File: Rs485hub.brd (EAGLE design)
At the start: 100 x 100 mm, 97 parts, among them IC1 SN75176PA, IC2 74AC00N, IC3 SN75176PA, IC4 74AC00N, IC5 SN75176PA, IC6 74AC00N, IC7 SN75176PA, IC8 74AC00N

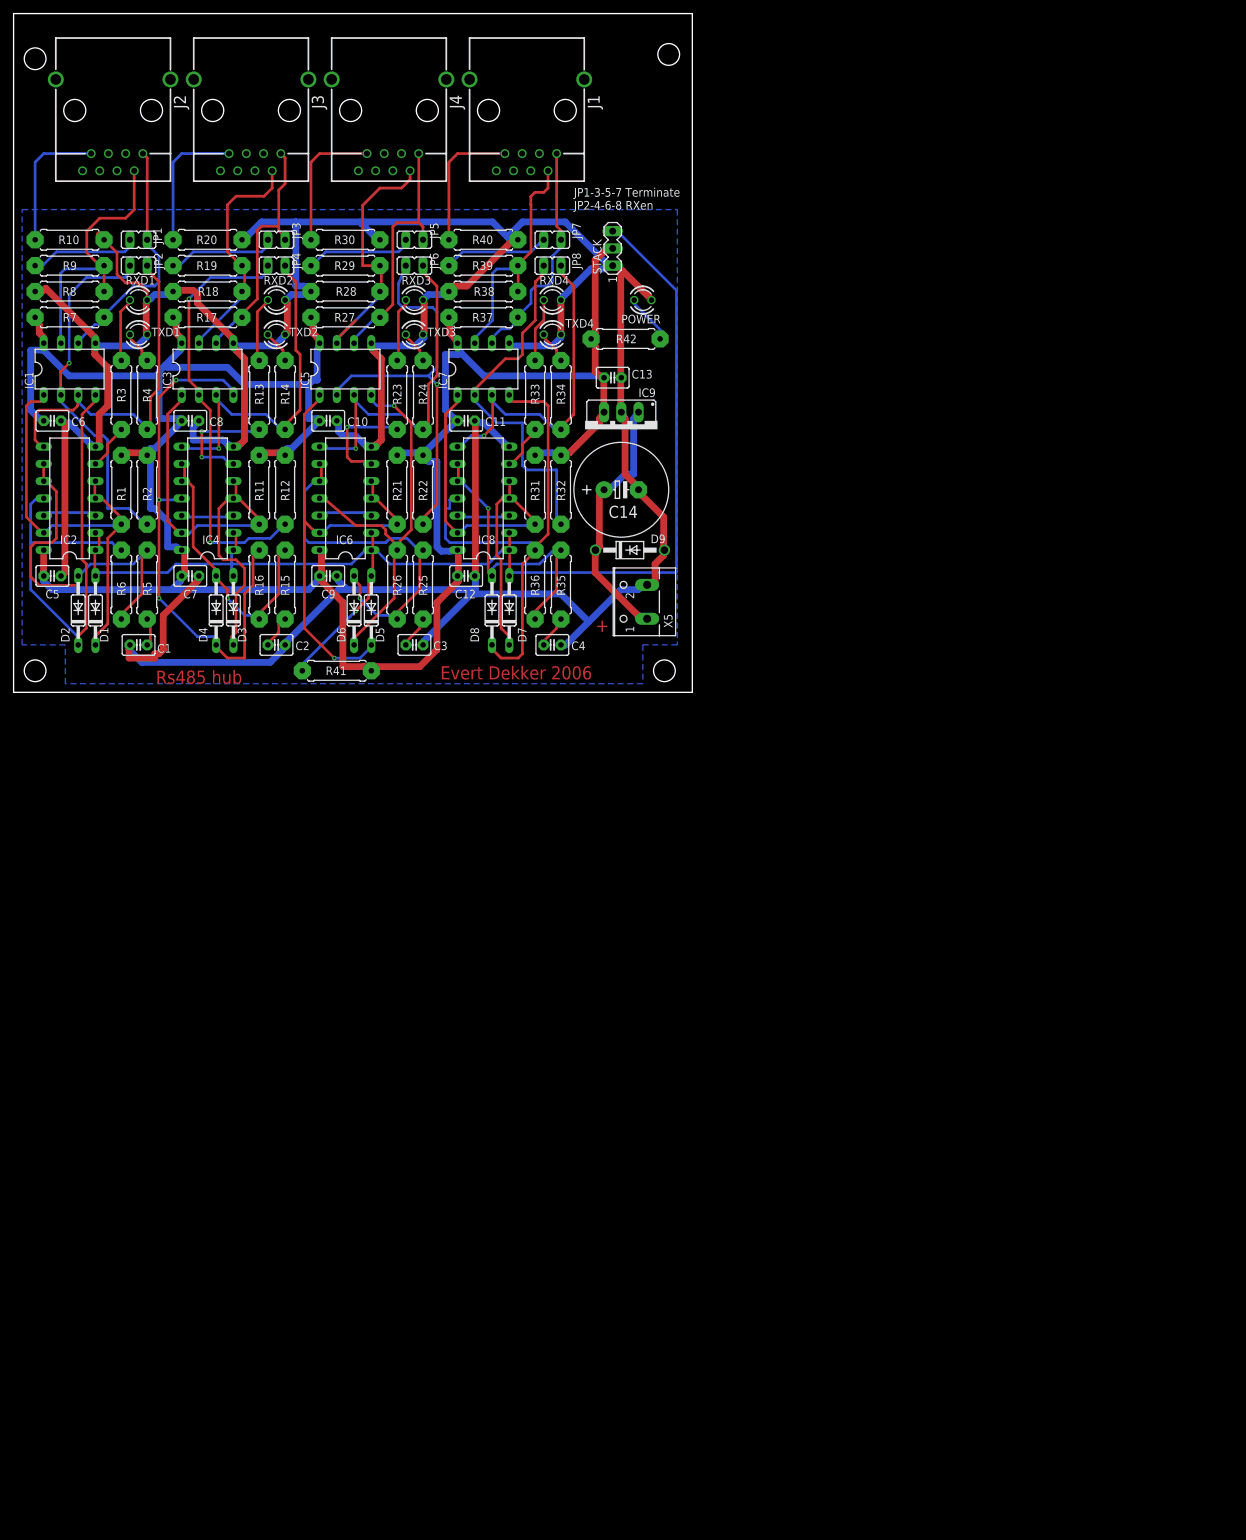
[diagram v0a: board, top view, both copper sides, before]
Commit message: Further mods for the 19" rack at RaumZeitLabor, still needs routing
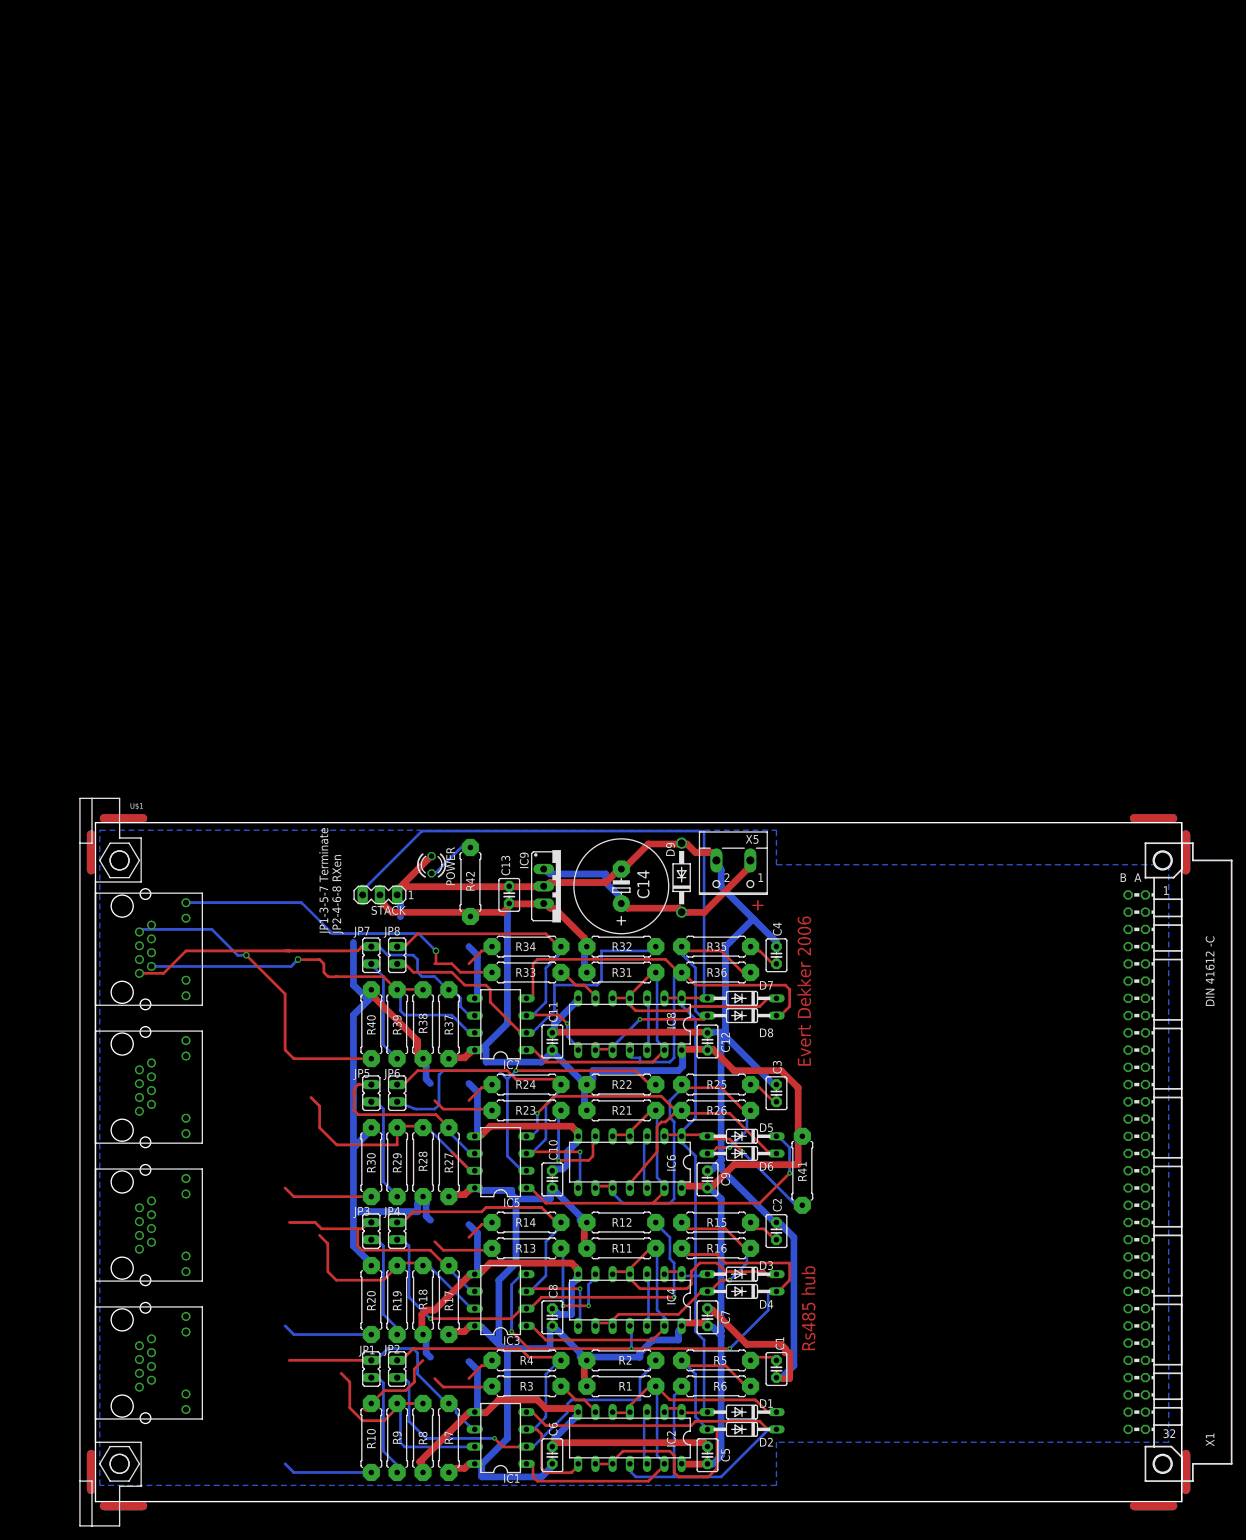
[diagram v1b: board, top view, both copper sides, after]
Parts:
- removed J1, J2, J3, J4: (no value), con-amp:557786-1
- removed RXD1, RXD2, RXD3, RXD4: Grn rxd, led:LED3MM
- removed TXD1, TXD2, TXD3, TXD4: red txd, led:LED3MM
- added U$1: (no value), 19inch:EK-FP
- added U$2, U$3, U$4, U$5: RJHS508, RJHS:P-RJHS-538X
- added X1: MAB64, con-vg:MAB64
- moved R10 182.0 mm to (52.7, -109.9), turned to 90 degrees
- moved R9 179.3 mm to (56.5, -109.9), turned to 90 degrees
- moved R8 176.8 mm to (60.3, -109.9), turned to 270 degrees
- moved R7 174.3 mm to (64.1, -109.9), turned to 90 degrees
- moved JP1 169.9 mm to (52.7, -99.7), turned to 180 degrees
- moved IC1 169.8 mm to (71.8, -109.9), turned to 90 degrees
- moved C6 169.3 mm to (79.4, -112.4), turned to 90 degrees
- moved JP2 167.0 mm to (56.5, -99.7), turned to 180 degrees
- moved C5 161.5 mm to (102.2, -112.4), turned to 90 degrees
- moved IC2 161.2 mm to (90.8, -109.9), turned to 180 degrees
- moved R20 158.1 mm to (52.7, -89.5), turned to 90 degrees
- moved R3 157.8 mm to (75.6, -102.2), turned to 0 degrees
- moved D2 155.3 mm to (107.3, -108.6), turned to 180 degrees
- moved R19 154.9 mm to (56.5, -89.5), turned to 90 degrees
- moved R4 152.8 mm to (75.6, -98.4), turned to 0 degrees
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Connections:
- net GND: now also U$2.P1K, U$2.P2K, U$3.P1K, U$3.P2K, U$4.P1K, U$4.P2K, U$5.P1K, U$5.P2K, X1.A29; no longer RXD1.K, RXD2.K, RXD3.K, RXD4.K, TXD1.K, TXD2.K, TXD3.K, TXD4.K
- net N$1: now also U$2.P2A; no longer TXD1.A
- net N$10: now also U$2.P1; no longer J2.1-1
- net N$17: now also U$3.P1A; no longer RXD2.A
- net N$18: now also U$3.P2; no longer J3.1-2
- net N$2: now also U$2.P1A; no longer RXD1.A
- net N$20: now also U$3.P1; no longer J3.1-1
- net N$21: now also U$5.P1; no longer J1.1-1
- net N$3: now also U$2.P7; no longer J2.1-7
- net N$30: now also U$3.P7; no longer J3.1-7
- net N$31: now also U$4.P2A; no longer TXD3.A
- net N$32: now also U$4.P1A; no longer RXD3.A
- net N$33: now also U$4.P2; no longer J4.1-2
- net N$35: now also U$4.P1; no longer J4.1-1
- net N$4: now also U$2.P2; no longer J2.1-2
- net N$45: now also U$4.P7; no longer J4.1-7
- net N$46: now also U$5.P2A; no longer TXD4.A
- net N$47: now also U$5.P1A; no longer RXD4.A
- net N$48: now also U$5.P2; no longer J1.1-2
- net N$6: now also U$3.P2A; no longer TXD2.A
- net N$60: now also U$5.P7; no longer J1.1-7
- net VCC: now also X1.A1, X1.A32
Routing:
- net N$47: track 9.41 -> 50.6 mm, vias 0 -> 1
- net GND: track 521.3 -> 481.1 mm
- net N$60: track 20.2 -> 47.0 mm, vias 0 -> 1
- net N$21: track 34.1 -> 57.6 mm
- net N$48: track 35.8 -> 58.5 mm, vias 0 -> 1
- net N$35: track 37.9 -> 27.8 mm
- net N$45: track 20.2 -> 13.2 mm
- net N$30: track 20.2 -> 13.2 mm
- net N$3: track 20.2 -> 13.2 mm
- net N$4: track 41.4 -> 35.7 mm
- net N$18: track 34.1 -> 31.6 mm
- net N$33: track 39.7 -> 38.4 mm
- net N$20: track 36.2 -> 35.3 mm
- net N$10: track 35.8 -> 34.9 mm
- net N$17: track 9.54 -> 9.01 mm
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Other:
- board size 100 x 100 mm -> 160 x 100 mm

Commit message: Added routing ;)
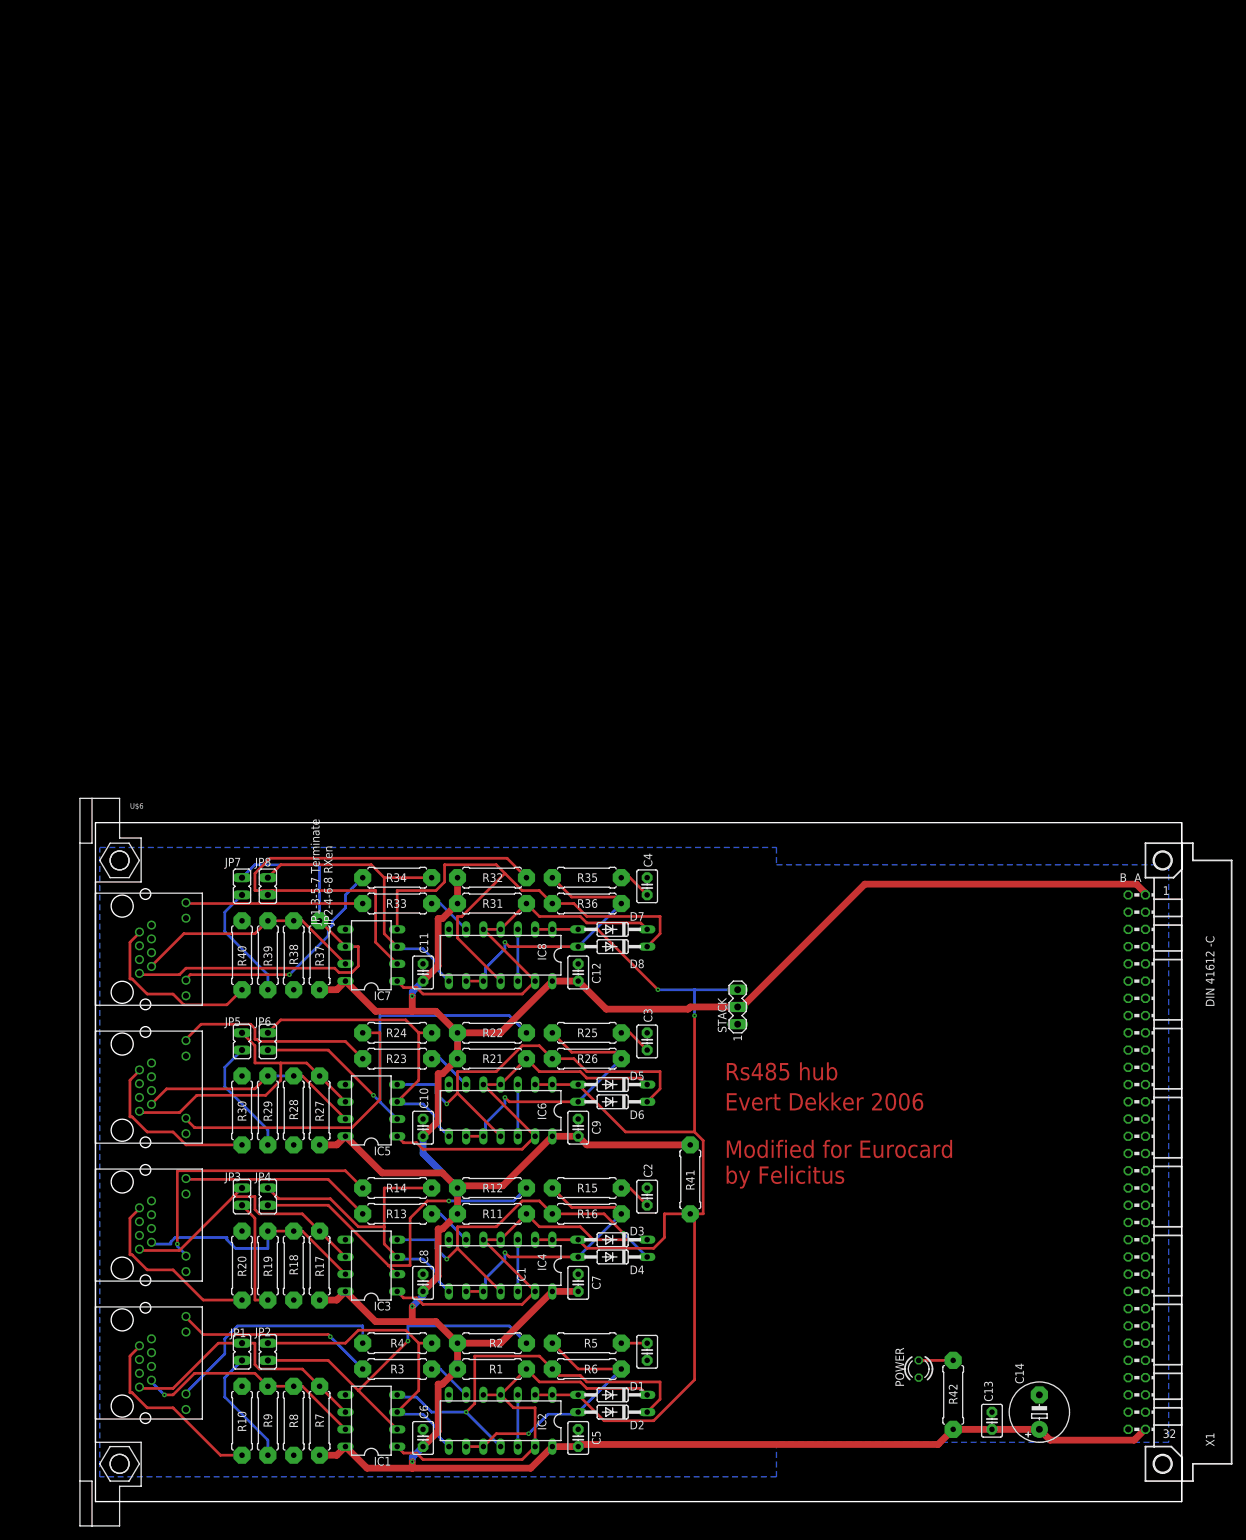
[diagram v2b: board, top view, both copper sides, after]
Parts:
- removed D9: 1N4004, diode:DO41-10
- removed IC9: (no value), v-reg:78XXS
- removed X5: (no value), con-wago-500:W237-102
- C14: value 1000u/16v -> (none); device rcl:E5-13 -> rcl:E5-8,5
- moved C13 105.2 mm to (144.1, -107.3)
- moved R42 103.8 mm to (138.4, -103.5)
- moved POWER 103.3 mm to (133.3, -99.7), turned to 270 degrees
- moved C14 99.0 mm to (151.1, -106.0)
- moved STACK 55.2 mm to (106.7, -46.4), turned to 90 degrees
- moved IC8 21.6 mm to (71.8, -38.7)
- moved R37 21.6 mm to (45.1, -38.7)
- moved R38 21.6 mm to (41.3, -38.7)
- moved C11 21.6 mm to (60.3, -41.3)
- moved C12 21.6 mm to (83.2, -41.3)
- moved D7 21.6 mm to (88.3, -34.9)
- moved IC7 21.6 mm to (52.7, -38.7)
- moved R32 21.6 mm to (70.5, -27.3)
- moved R34 21.6 mm to (56.5, -27.3)
- moved R35 21.6 mm to (84.5, -27.3)
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- renumbered U$1 to U$6
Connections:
- removed net N$7: C14.+, D9.C, IC9.IN, X5.1
- net GND: no longer D9.A, IC9.GND, X5.2
- net VCC: now also C14.+; no longer IC9.OUT
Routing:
- net GND: track 481.1 -> 0.00 mm
- net VCC: track 351.7 -> 467.4 mm, vias 0 -> 3
- net N$31: track 4.30 -> 43.3 mm
- net N$7: track 37.7 -> 0.00 mm
- net N$6: track 4.24 -> 41.5 mm, vias 0 -> 1
- net N$46: track 4.39 -> 34.5 mm, vias 0 -> 1
- net N$1: track 4.48 -> 34.1 mm
- net N$47: track 50.6 -> 26.2 mm, vias 1 -> 0
- net N$48: track 58.5 -> 34.0 mm, vias 1 -> 0
- net N$27: track 79.9 -> 56.6 mm, vias 3 -> 2
- net N$59: track 53.3 -> 75.4 mm
- net N$32: track 8.98 -> 30.2 mm
- net N$60: track 47.0 -> 26.5 mm, vias 1 -> 0
- net N$2: track 8.97 -> 29.3 mm, vias 0 -> 1
- net N$17: track 9.01 -> 28.3 mm
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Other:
- board text added: "Modified for Eurocard by Felicitus"
- board text removed: "+"
